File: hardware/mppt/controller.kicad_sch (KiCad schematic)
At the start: 39 parts, among them SW201 SW_SPST, U201 STM32F446RETx, Y201 16MHz, Y202 32kHz

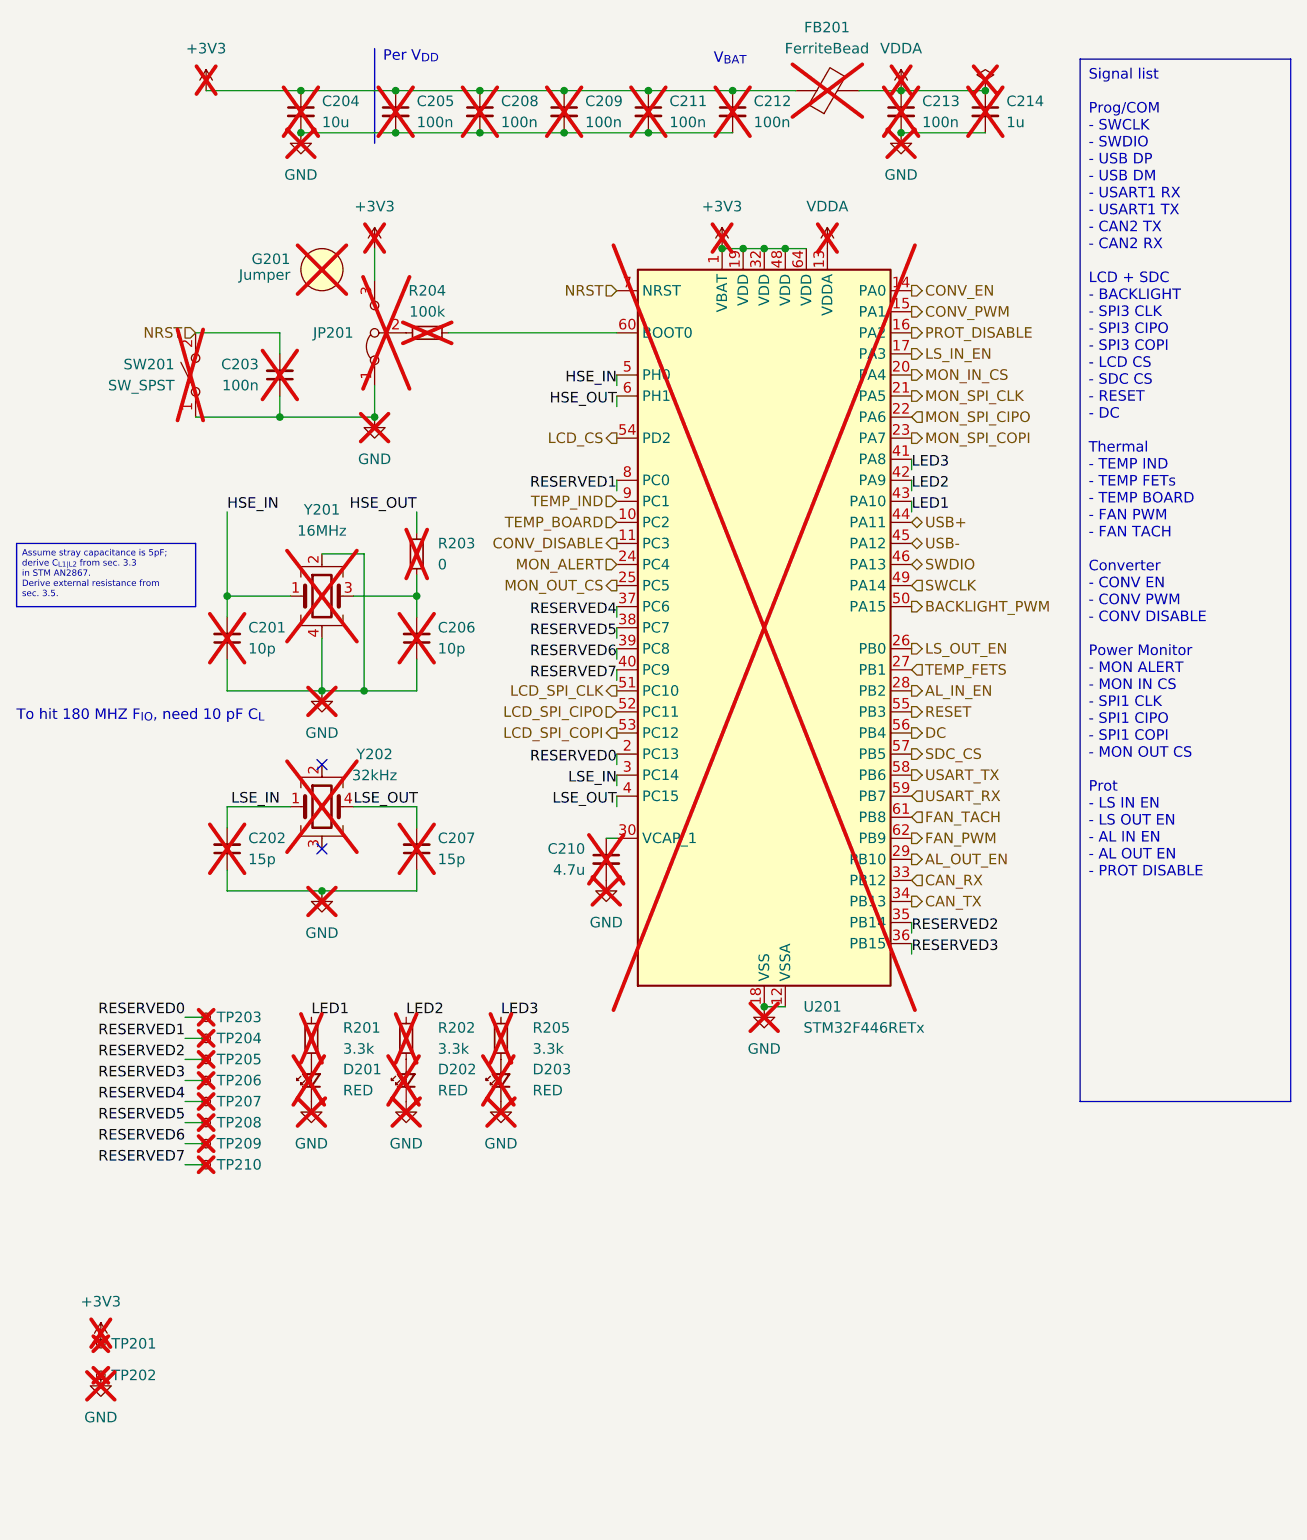
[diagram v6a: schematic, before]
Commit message: unset dnp for all components in sch
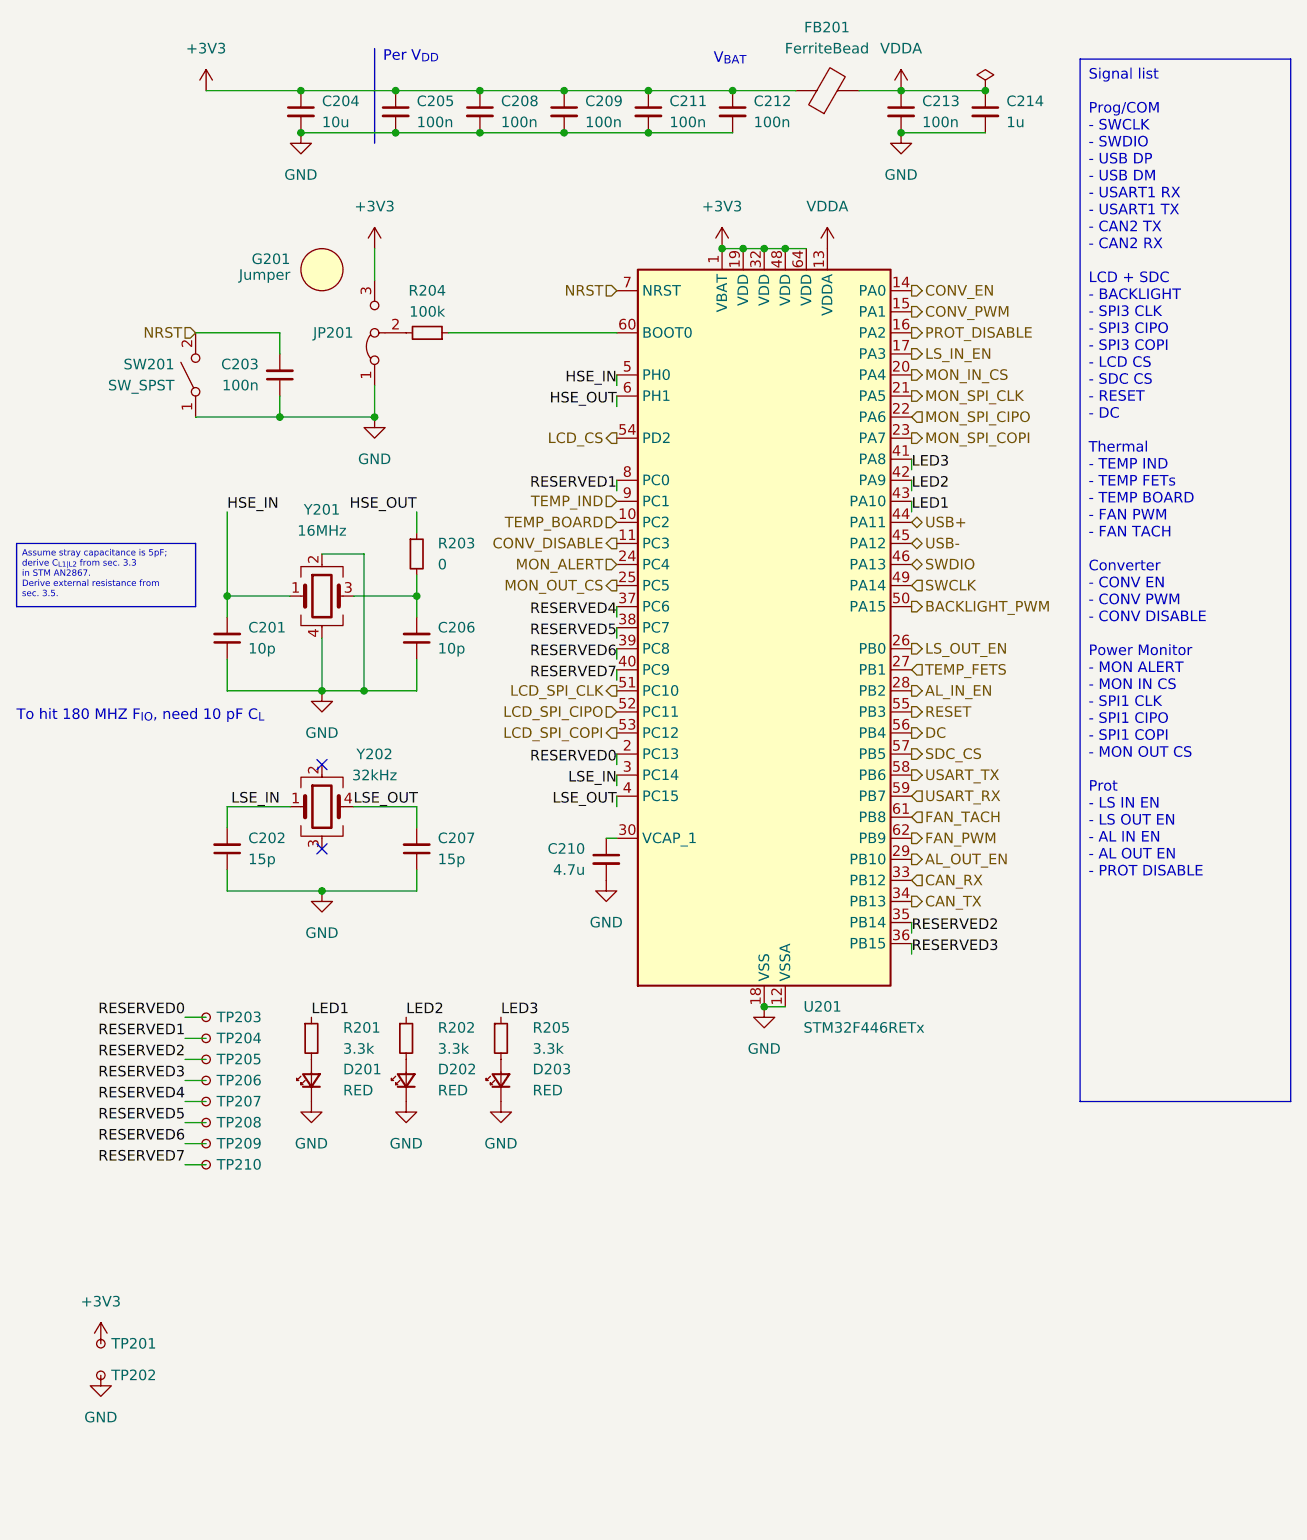
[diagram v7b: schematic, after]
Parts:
- C201, C202, C203, C204, C205, C206, C207, C208, C209, C210, C211, C212, C213, C214, D201, D202, D203, FB201, G201, JP201, R201, R202, R203, R204, R205, SW201, TP201, TP202, TP203, TP204, TP205, TP206, TP207, TP208, TP209, TP210, U201, Y201, Y202: now fitted; now in the parts list

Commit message: remove testpoints, integrat 60% of layout
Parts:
- C201, C206: footprint Capacitor_SMD:C_0402_1005Metric_Pad0.74x0.62mm_HandSolder -> Capacitor_SMD:C_0402_1005Metric; P/N CGA2B2C0G1H100D050BA -> CGA2B2C0G1H100D050BA
- C202, C207: footprint Capacitor_SMD:C_0402_1005Metric_Pad0.74x0.62mm_HandSolder -> Capacitor_SMD:C_0402_1005Metric
- C210: footprint Capacitor_SMD:C_0805_2012Metric_Pad1.18x1.45mm_HandSolder -> Capacitor_SMD:C_0603_1608Metric; P/N CGA4J1X7R1E475K125AC -> CGA3E1X7T1A475K080AC
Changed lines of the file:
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@@
 			)
 		)
-		(property "Footprint" "Capacitor_SMD:C_0402_1005Metric_Pad0.74x0.62mm_HandSolder"
+		(property "Footprint" "Capacitor_SMD:C_0402_1005Metric"
 			(at 40.64 116.84 0)
 			(effects
@@
 			)
 		)
-		(property "Footprint" "Capacitor_SMD:C_0402_1005Metric_Pad0.74x0.62mm_HandSolder"
+		(property "Footprint" "Capacitor_SMD:C_0402_1005Metric"
 			(at 40.64 91.44 0)
 			(effects
@@
 			)
 		)
-		(property "P/N" "CGA2B2C0G1H100D050BA "
+		(property "P/N" "CGA2B2C0G1H100D050BA"
 			(at 40.64 91.44 0)
 			(effects
@@
 			)
 		)
-		(property "Footprint" "Capacitor_SMD:C_0402_1005Metric_Pad0.74x0.62mm_HandSolder"
+		(property "Footprint" "Capacitor_SMD:C_0402_1005Metric"
 			(at 63.5 91.44 0)
 			(effects
@@
 			)
 		)
-		(property "P/N" "CGA2B2C0G1H100D050BA "
+		(property "P/N" "CGA2B2C0G1H100D050BA"
 			(at 63.5 91.44 0)
 			(effects
@@
 			)
 		)
-		(property "Footprint" "Capacitor_SMD:C_0402_1005Metric_Pad0.74x0.62mm_HandSolder"
+		(property "Footprint" "Capacitor_SMD:C_0402_1005Metric"
 			(at 63.5 116.84 0)
 			(effects
@@
 			)
 		)
-		(property "Footprint" "Capacitor_SMD:C_0805_2012Metric_Pad1.18x1.45mm_HandSolder"
+		(property "Footprint" "Capacitor_SMD:C_0603_1608Metric"
 			(at 86.36 118.11 0)
 			(effects
@@
 			)
 		)
-		(property "Datasheet" "https://product.tdk.com/en/search/capacitor/ceramic/mlcc/info?part_no=CGA4J1X7R1E475K125AC"
+		(property "Datasheet" "https://product.tdk.com/en/search/capacitor/ceramic/mlcc/info?part_no=CGA3E1X7T1A475K080AC"
 			(at 86.36 118.11 0)
 			(effects
@@
 			)
 		)
-		(property "P/N" "CGA4J1X7R1E475K125AC "
+		(property "P/N" "CGA3E1X7T1A475K080AC"
 			(at 86.36 118.11 0)
 			(effects
